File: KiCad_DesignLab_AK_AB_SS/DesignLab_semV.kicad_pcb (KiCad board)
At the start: 2 copper layers, 24 x 16 mm, 16 parts, among them U1 ATmega328PB-A, U2 AMS1117-3.3, U3 CC56-12EWA, U5 SDcard_Reader, Y1 Crystal

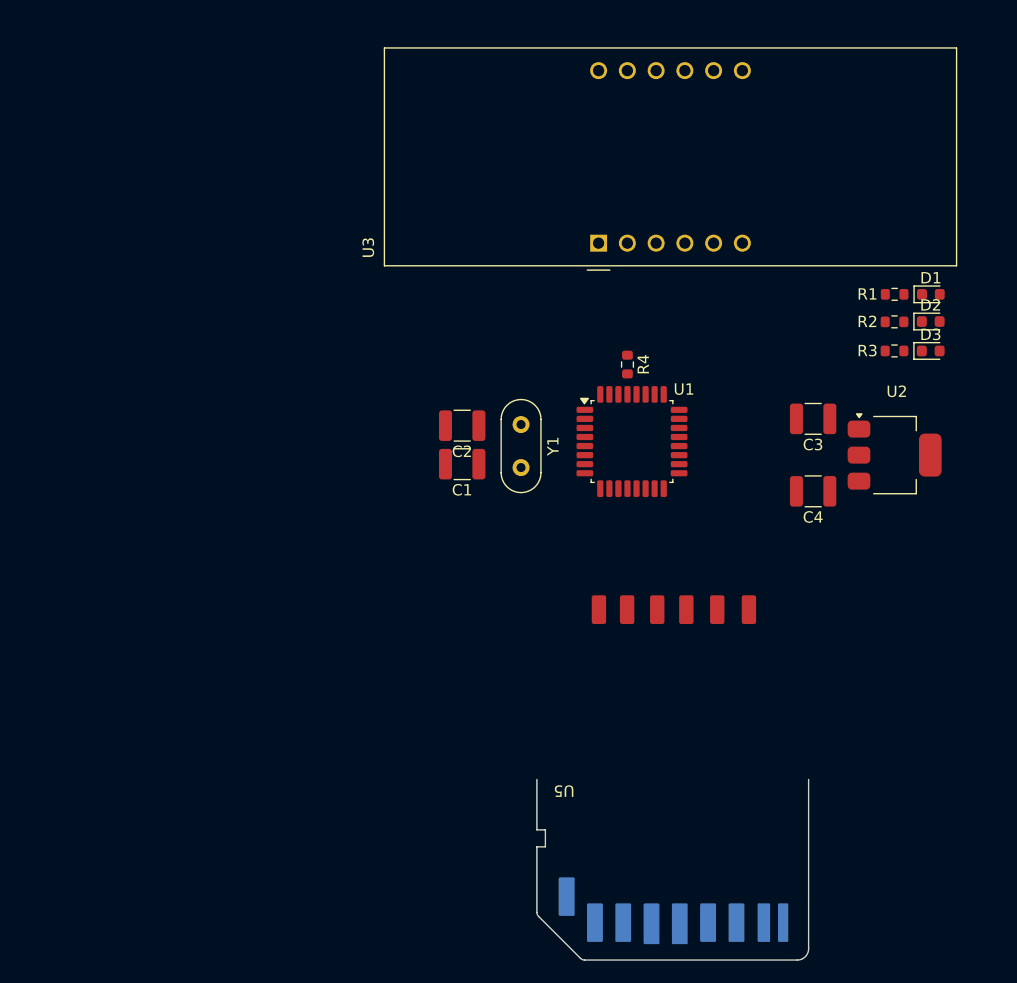
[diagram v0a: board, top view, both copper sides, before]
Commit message: Routed power lines
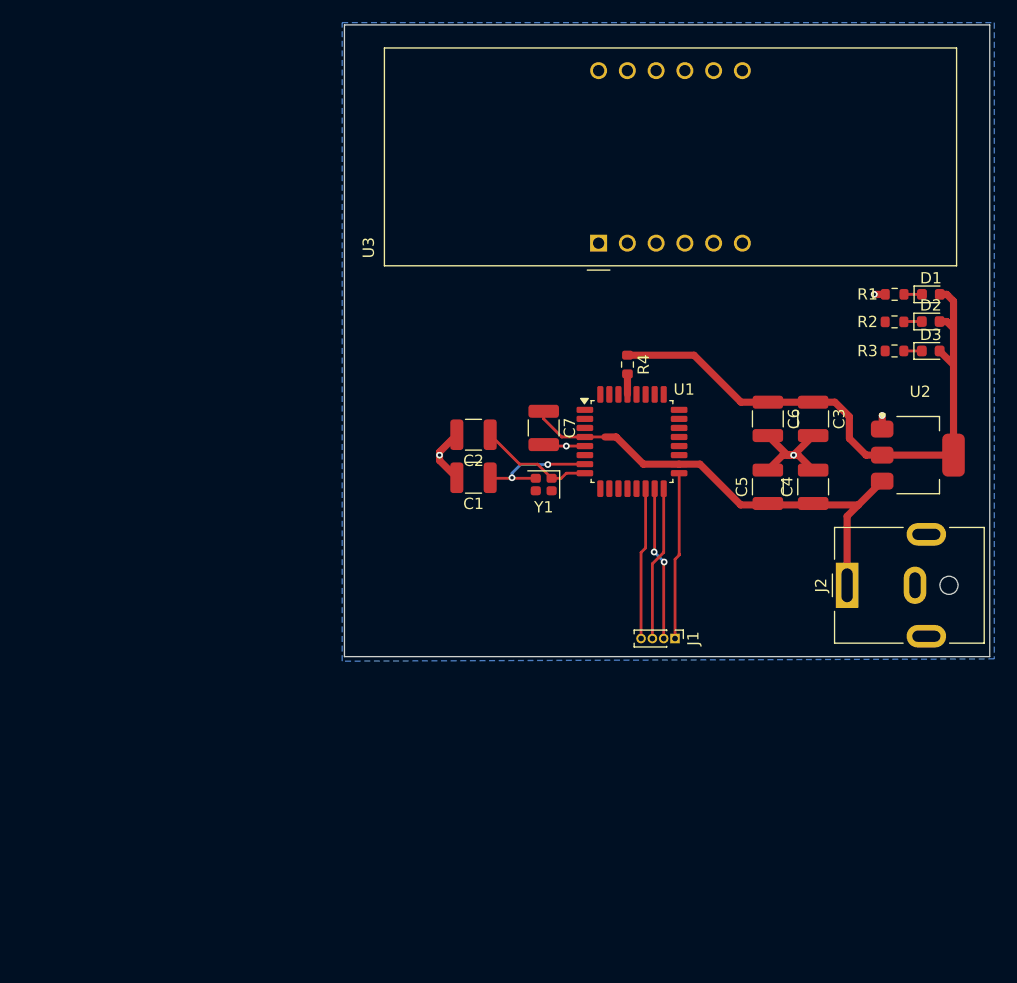
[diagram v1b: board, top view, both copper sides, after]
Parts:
- removed U5: SDcard_Reader, Custom_footprints:SD_Card_Device_custom
- added C5: 100n, Capacitor_SMD:C_1210_3225Metric, F.Cu at (144.6, 93.2)
- added C6: 100n, Capacitor_SMD:C_1210_3225Metric, F.Cu at (144.6, 87.2)
- added C7: 100n, Capacitor_SMD:C_1210_3225Metric, F.Cu at (124.8, 88.0)
- added J1: Conn_01x04_Pin, Connector_PinHeader_1.00mm:PinHeader_1x04_P1.00mm_Vertical, F.Cu at (136.4, 106.6)
- added J2: Barrel_Jack_MountingPin, Connector_BarrelJack:BarrelJack_CUI_PJ-063AH_Horizontal, F.Cu at (151.6, 101.9)
- Y1: footprint Crystal:Crystal_HC52-U_Vertical -> Crystal:Crystal_SMD_2016-4Pin_2.0x1.6mm
- moved Y1 5.66 mm to (124.8, 93.0), turned to 180 degrees
- moved U2 2.05 mm to (157.8, 90.4)
- moved C1 1.56 mm to (118.6, 92.4)
- moved C2 1.28 mm to (118.6, 88.6)
- moved C4 0.40 mm to (148.6, 93.2), turned to 90 degrees
- turned C3 to -90 degrees
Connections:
- U1 pad 14: Net-(U1-PB2) -> CS
- U1 pad 15: Net-(U1-PB3) -> MOSI
- U1 pad 16: Net-(U1-PB4) -> MISO
- U1 pad 17: Net-(U1-PB5) -> SCK
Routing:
- net 3.3V: track 0.00 -> 51.9 mm
- net 5V: track 0.00 -> 42.1 mm
- net GND: track 0.00 -> 21.5 mm, vias 0 -> 5
- net SCK: track 0.00 -> 14.8 mm
- net MOSI: track 0.00 -> 13.7 mm, vias 0 -> 2
- net MISO: track 0.00 -> 13.7 mm
- net CS: track 0.00 -> 13.4 mm
- net Net-(U1-XTAL1/PB6): track 0.00 -> 11.2 mm, vias 0 -> 2
- net Net-(U1-XTAL2/PB7): track 0.00 -> 10.1 mm
- net Net-(U1-~{RESET}/PC6): track 0.00 -> 1.81 mm
- net Net-(D2-K): track 0.00 -> 1.60 mm
- net Net-(D1-K): track 0.00 -> 1.59 mm
- net Net-(D3-K): track 0.00 -> 1.59 mm
- added copper zone on B.Cu, net GND
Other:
- board size 24 x 16 mm -> 57 x 55.8 mm

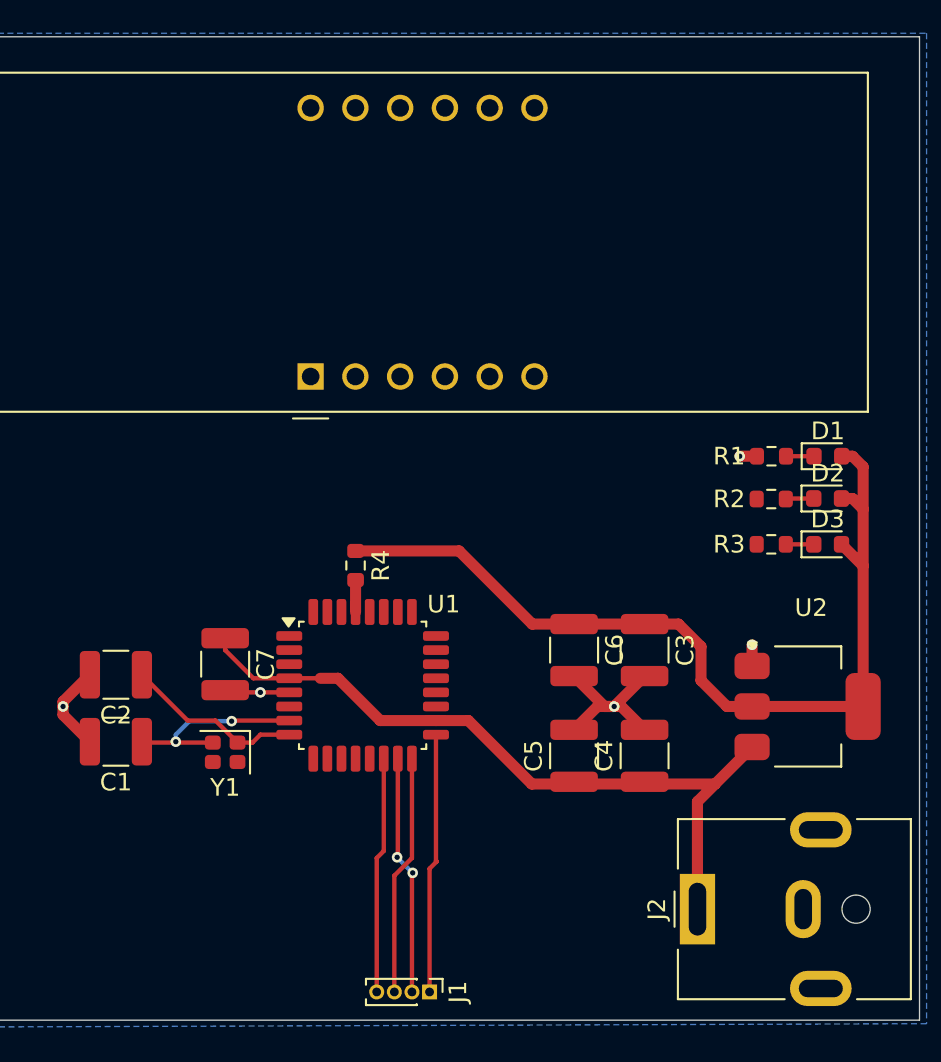
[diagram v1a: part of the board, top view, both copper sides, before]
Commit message: Finished routing the PCB
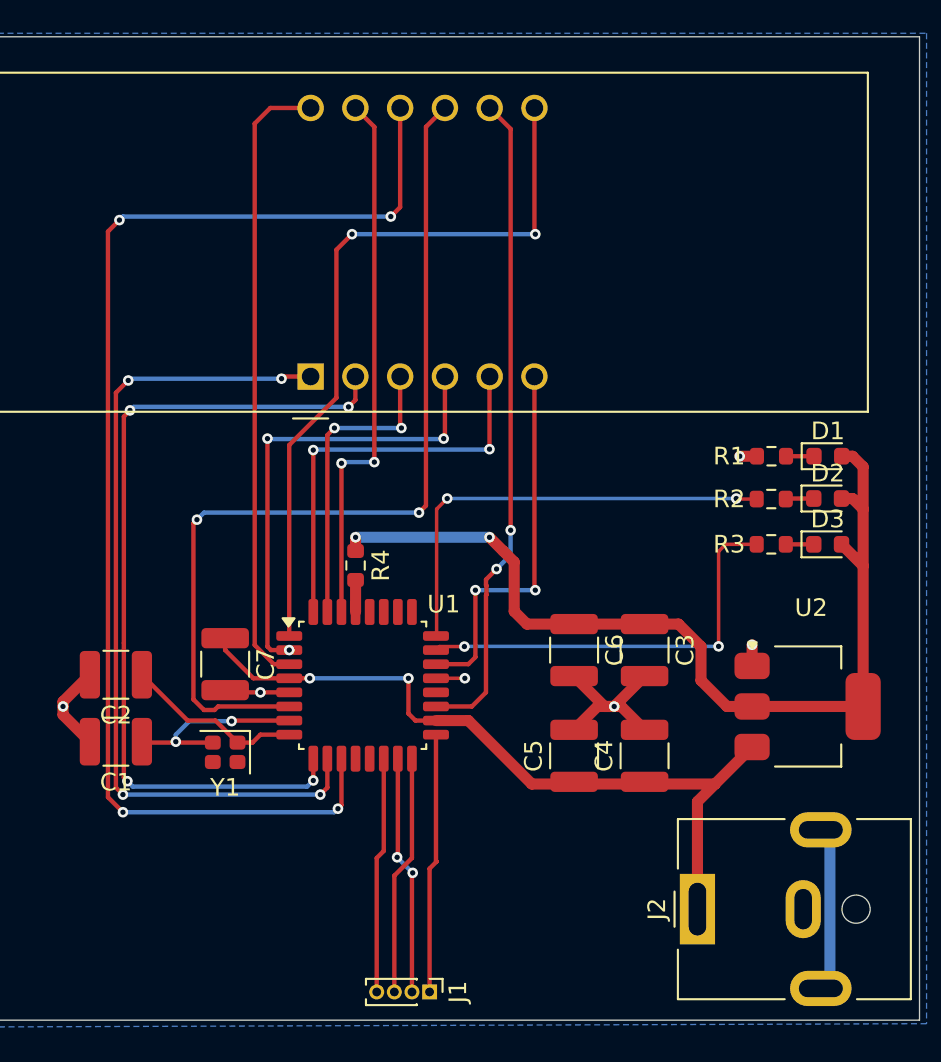
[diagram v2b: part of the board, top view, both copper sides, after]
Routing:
- net Net-(U1-PD7): track 0.00 -> 71.3 mm, vias 0 -> 4
- net CC2: track 0.00 -> 52.4 mm, vias 0 -> 2
- net Net-(U1-PD6): track 0.00 -> 47.8 mm, vias 0 -> 4
- net Net-(U1-PD5): track 0.00 -> 47.7 mm, vias 0 -> 4
- net Net-(U1-PD3): track 0.00 -> 41.9 mm, vias 0 -> 2
- net CC3: track 0.00 -> 37.4 mm, vias 0 -> 2
- net CC1: track 0.00 -> 35.5 mm
- net Net-(U1-PD0): track 0.00 -> 30.9 mm, vias 0 -> 2
- net Net-(U1-PD4): track 0.00 -> 26.7 mm, vias 0 -> 3
- net LED_SPI: track 0.00 -> 25.6 mm, vias 0 -> 2
- net LED_UART: track 0.00 -> 23.8 mm, vias 0 -> 2
- net Net-(U1-PD2): track 0.00 -> 23.4 mm, vias 0 -> 2
- net CC4: track 0.00 -> 21.7 mm, vias 0 -> 2
- net Net-(U1-PD1): track 0.00 -> 17.4 mm, vias 0 -> 2
- net unconnected-(J2-MountPin-PadMP): track 0.00 -> 9.43 mm
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
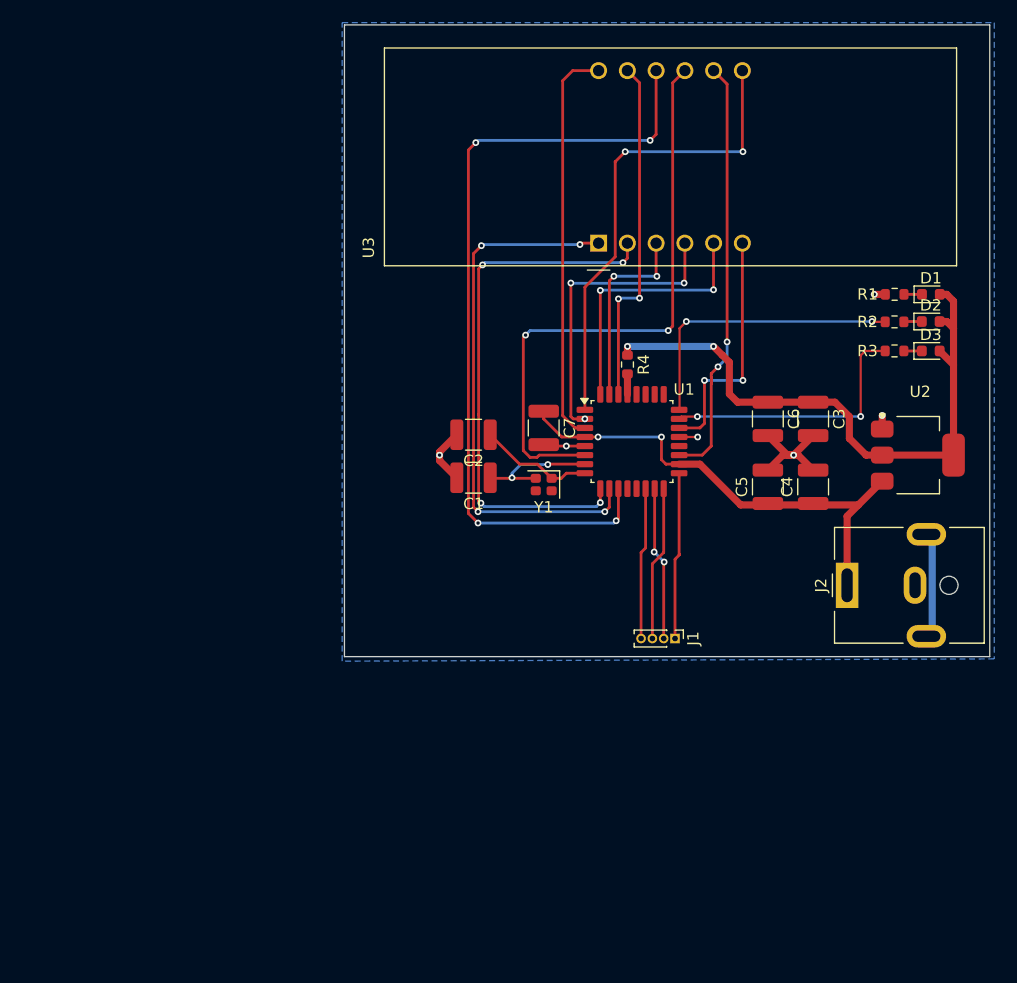
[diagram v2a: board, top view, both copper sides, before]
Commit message: Fixed schematic + footprints
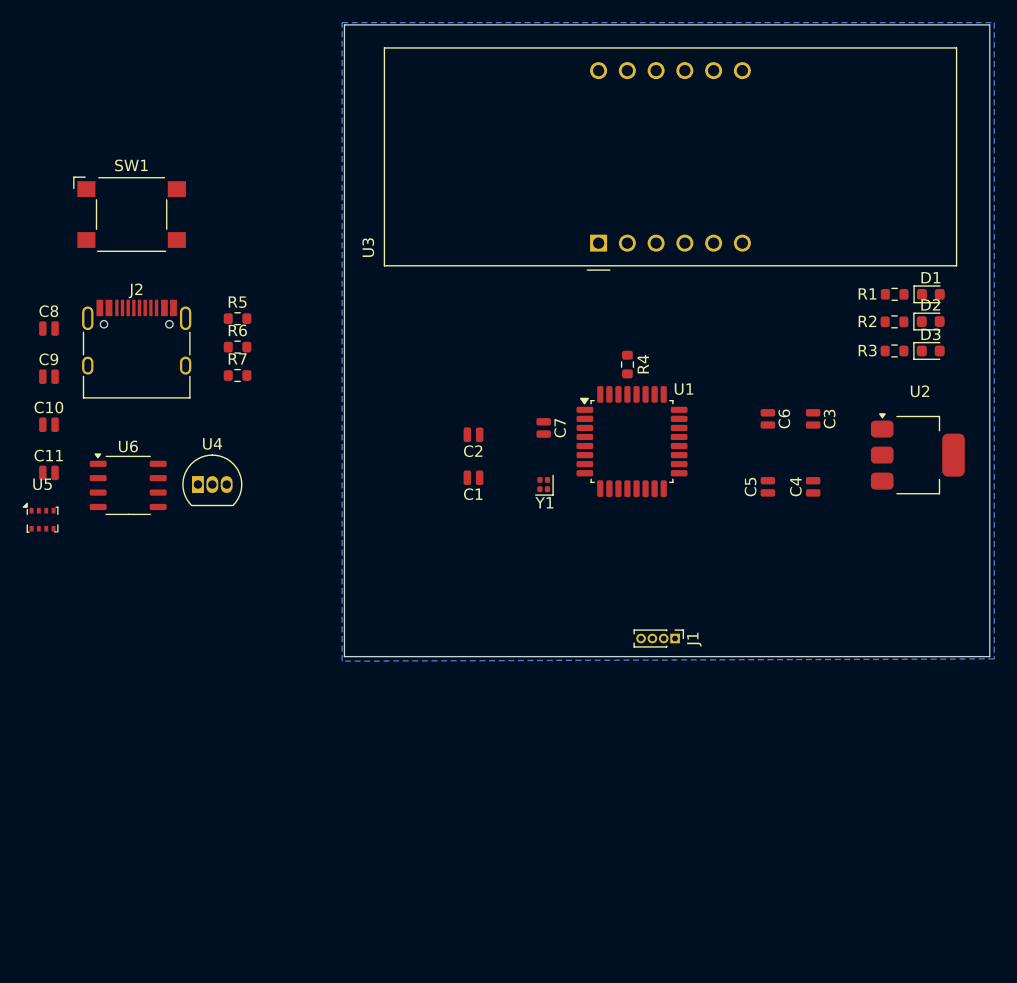
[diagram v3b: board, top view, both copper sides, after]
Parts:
- added C10: 100n, Capacitor_SMD:C_0504_1310Metric, F.Cu at (81.1, 87.7)
- added C11: 100n, Capacitor_SMD:C_0504_1310Metric, F.Cu at (81.1, 92.0)
- added C8: 1n, Capacitor_SMD:C_0504_1310Metric, F.Cu at (81.1, 79.2)
- added C9: 100n, Capacitor_SMD:C_0504_1310Metric, F.Cu at (81.1, 83.5)
- added R5: 5.1k, Resistor_SMD:R_0603_1608Metric, F.Cu at (97.8, 78.3)
- added R6: 5.1k, Resistor_SMD:R_0603_1608Metric, F.Cu at (97.8, 80.9)
- added R7: 1k, Resistor_SMD:R_0603_1608Metric, F.Cu at (97.8, 83.4)
- added SW1: SW_Omron_B3FS, Button_Switch_SMD:SW_SPST_Omron_B3FS-100xP, F.Cu at (88.4, 69.2)
- added U4: DS18B20, Package_TO_SOT_THT:TO-92_Inline, F.Cu at (94.3, 93.0)
- added U5: BMP280, Package_LGA:Bosch_LGA-8_2x2.5mm_P0.65mm_ClockwisePinNumbering, F.Cu at (80.5, 96.1)
- added U6: CH340N, Package_SO:JEITA_SOIC-8_3.9x4.9mm_P1.27mm, F.Cu at (88.1, 93.1)
- C1, C2, C3, C4, C5, C6, C7: footprint Capacitor_SMD:C_1210_3225Metric -> Capacitor_SMD:C_0504_1310Metric
- J2: value Barrel_Jack_MountingPin -> USB_C_Receptacle_USB2.0_16P; footprint Connector_BarrelJack:BarrelJack_CUI_PJ-063AH_Horizontal -> Connector_USB:USB_C_Receptacle_HRO_TYPE-C-31-M-12
- Y1: footprint Crystal:Crystal_SMD_2016-4Pin_2.0x1.6mm -> Crystal:Crystal_SMD_1210-4Pin_1.2x1.0mm
- moved J2 66.0 mm to (88.8, 81.4), turned to 0 degrees
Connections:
- net CC3 renamed Net-(U1-PE2)
- net CC4 renamed Net-(U1-PE3)
- net Net-(U1-PD2) renamed G
- net Net-(U1-PD3) renamed B
- net Net-(U1-PD4) renamed C
- net Net-(U1-PD5) renamed D
- net Net-(U1-PD6) renamed E
- net Net-(U1-PD7) renamed F
- net Net-(U1-XTAL1/PB6) renamed XTAL1
- net Net-(U1-XTAL2/PB7) renamed XTAL2
- C4 pad 1: 5V -> 3.3V
- C5 pad 1: 5V -> 3.3V
- C7 pad 1: 5V -> 3.3V
- U1 pad 12: unconnected-(U1-PB0-Pad12) -> A
- U1 pad 13: unconnected-(U1-PB1-Pad13) -> DPX
- U1 pad 18: 5V -> 3.3V
- U1 pad 25: unconnected-(U1-PC2-Pad25) -> SW1
- U1 pad 26: unconnected-(U1-PC3-Pad26) -> 1W
- U1 pad 27: unconnected-(U1-PC4-Pad27) -> SDA
- U1 pad 28: unconnected-(U1-PC5-Pad28) -> SCL
- U1 pad 3: CC1 -> Net-(U1-PE0)
- U1 pad 30: Net-(U1-PD0) -> UART_RX
- U1 pad 31: Net-(U1-PD1) -> UART_TX
- U1 pad 4: 5V -> 3.3V
- U1 pad 6: CC2 -> Net-(U1-PE1)
- U2 pad 3: 5V -> 3.3V
- U3 pad 11: Net-(U1-PD0) -> A
- U3 pad 12: CC1 -> Net-(U1-PE0)
- U3 pad 3: Net-(U1-PD1) -> DPX
- U3 pad 9: CC2 -> Net-(U1-PE1)
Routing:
- net F: track 71.3 -> 0.00 mm, vias 4 -> 0
- net 3.3V: track 54.6 -> 0.00 mm, vias 2 -> 0
- net CC2: track 52.4 -> 0.00 mm, vias 2 -> 0
- net E: track 47.8 -> 0.00 mm, vias 4 -> 0
- net D: track 47.7 -> 0.00 mm, vias 4 -> 0
- net 5V: track 43.3 -> 0.00 mm, vias 2 -> 0
- net B: track 41.9 -> 0.00 mm, vias 2 -> 0
- net Net-(U1-PE2): track 37.4 -> 0.00 mm, vias 2 -> 0
- net CC1: track 35.5 -> 0.00 mm
- net Net-(U1-PD0): track 30.9 -> 0.00 mm, vias 2 -> 0
- net C: track 26.7 -> 0.00 mm, vias 3 -> 0
- net LED_SPI: track 25.6 -> 0.00 mm, vias 2 -> 0
- net LED_UART: track 23.8 -> 0.00 mm, vias 2 -> 0
- net G: track 23.4 -> 0.00 mm, vias 2 -> 0
- net GND: track 23.1 -> 0.00 mm, vias 6 -> 0
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
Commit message: Layout before routing
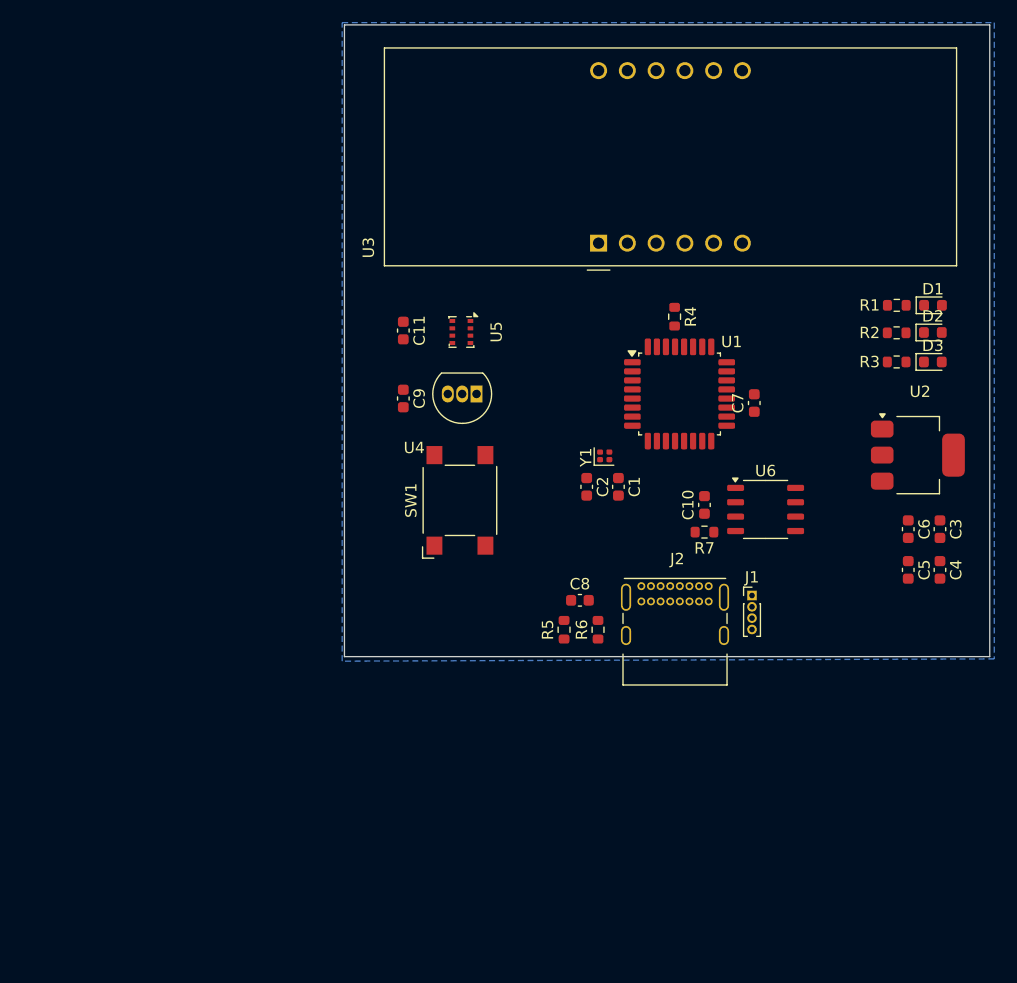
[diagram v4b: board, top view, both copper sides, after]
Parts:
- C1, C10, C11, C2, C3, C4, C5, C6, C7, C8, C9: footprint Capacitor_SMD:C_0504_1310Metric -> Capacitor_SMD:C_0603_1608Metric
- J2: footprint Connector_USB:USB_C_Receptacle_HRO_TYPE-C-31-M-12 -> Connector_USB:USB_C_Receptacle_GCT_USB4085
- moved C10 58.3 mm to (139.0, 94.8), turned to 90 degrees
- moved U6 56.3 mm to (144.4, 95.2)
- moved C8 52.7 mm to (128.0, 103.2)
- moved J2 49.1 mm to (133.4, 102.0)
- moved R7 43.5 mm to (139.0, 97.2), turned to 180 degrees
- moved U5 40.5 mm to (117.5, 79.5), turned to -90 degrees
- moved R6 40.5 mm to (129.6, 105.8), turned to 90 degrees
- moved R5 39.8 mm to (126.6, 105.8), turned to 90 degrees
- moved SW1 38.5 mm to (117.4, 94.4), turned to 90 degrees
- moved C11 33.7 mm to (112.4, 79.4), turned to -90 degrees
- moved C9 31.4 mm to (112.4, 85.4), turned to -90 degrees
- moved U4 25.9 mm to (118.9, 85.0), turned to 180 degrees
- moved C7 18.7 mm to (143.4, 85.8), turned to 90 degrees
- moved C6 15.8 mm to (157.0, 96.9)
- moved C3 14.8 mm to (159.8, 96.9)
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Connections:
- C11 pad 1: 3.3V -> 5V
- C4 pad 1: 3.3V -> 5V
- C5 pad 1: 3.3V -> 5V
- C7 pad 1: 3.3V -> 5V
- J2 pad A4: 3.3V -> 5V
- J2 pad A9: 3.3V -> 5V
- J2 pad B4: 3.3V -> 5V
- J2 pad B9: 3.3V -> 5V
- U1 pad 18: 3.3V -> 5V
- U1 pad 4: 3.3V -> 5V
- U2 pad 3: 3.3V -> 5V
- U4 pad 3: 3.3V -> 5V
- U5 pad 2: 3.3V -> 5V
- U5 pad 5: 3.3V -> 5V
